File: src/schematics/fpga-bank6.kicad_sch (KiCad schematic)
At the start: 1 part

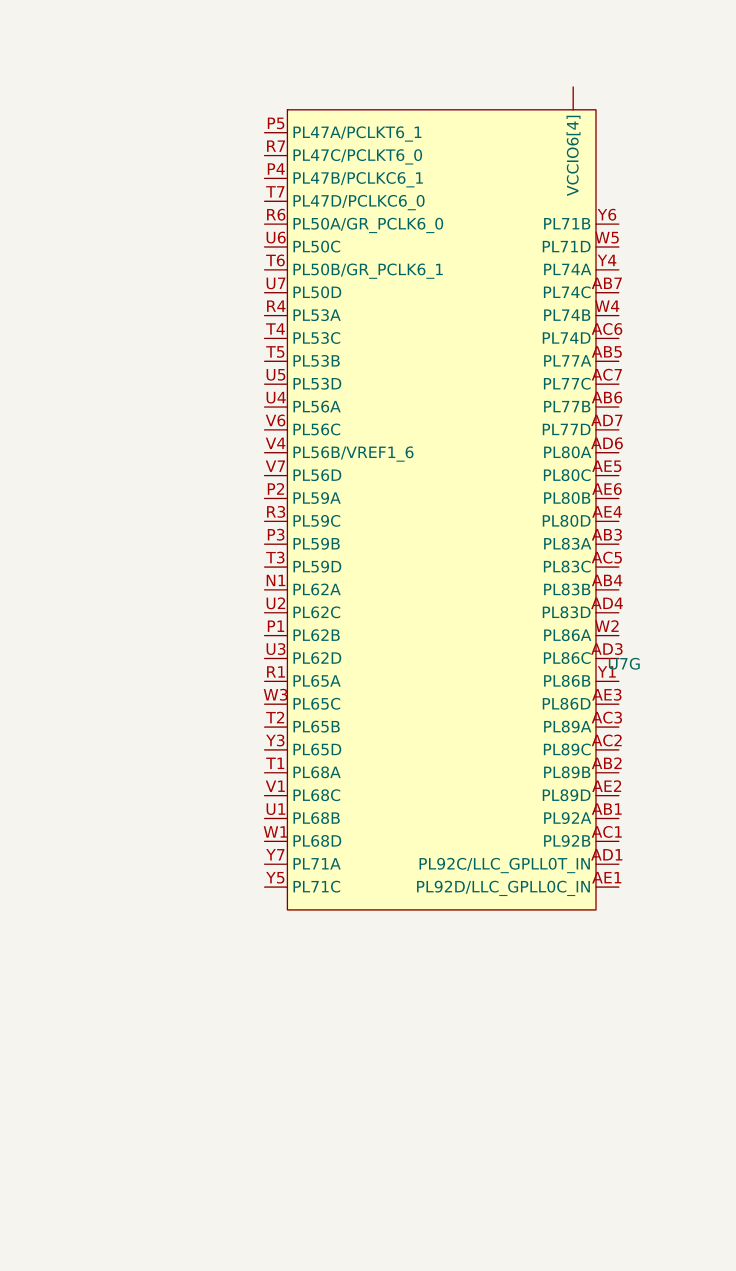
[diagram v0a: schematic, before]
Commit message: Draft connections between the FPGA and the memories
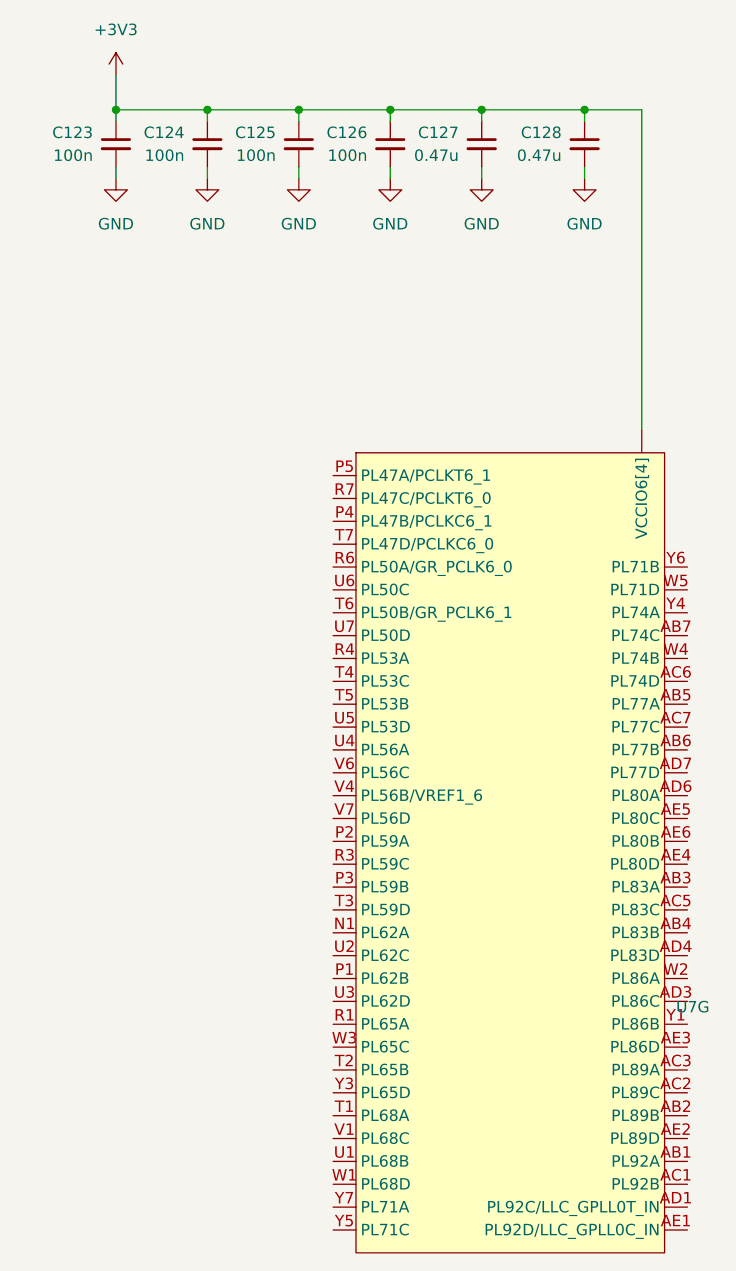
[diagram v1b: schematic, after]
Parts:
- added C123, C124, C125, C126: 100n, symbol Device:C_Small
- added C127, C128: 0.47u, symbol Device:C_Small
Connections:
- net VCCIO6 renamed +3V3
- net +3V3: now also C123.1, C124.1, C125.1, C126.1, C127.1, C128.1
- new net GND: C123.2, C124.2, C125.2, C126.2, C127.2, C128.2
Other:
- moved on the sheet: U7G

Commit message: Adds draft of IO connector schematic connections to FPGA
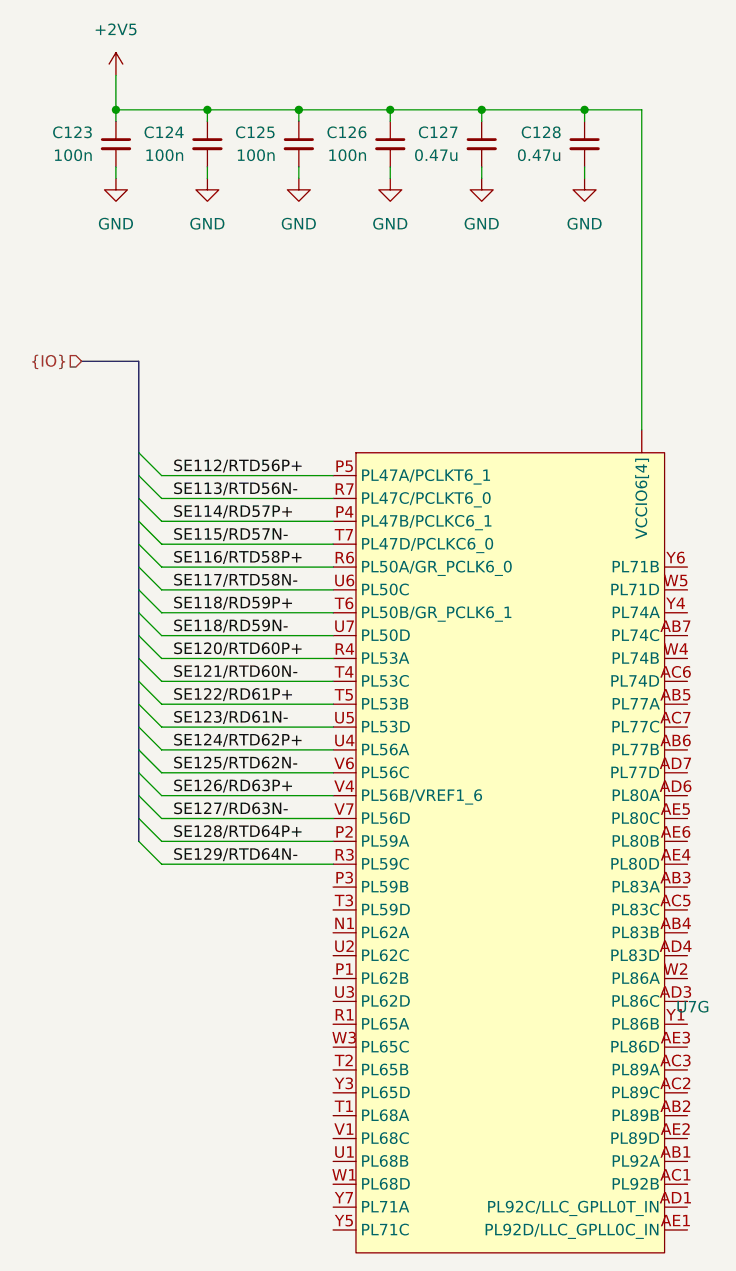
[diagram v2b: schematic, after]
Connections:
- net SE128/RTD64P+: now reaches U7.P2 (PL59A)
- net SE114/RD57P+: now reaches U7.P4 (PL47B/PCLKC6_1)
- net SE112/RTD56P+: now reaches U7.P5 (PL47A/PCLKT6_1)
- net SE129/RTD64N-: now reaches U7.R3 (PL59C)
- net SE120/RTD60P+: now reaches U7.R4 (PL53A)
- net SE116/RTD58P+: now reaches U7.R6 (PL50A/GR_PCLK6_0)
- net SE113/RTD56N-: now reaches U7.R7 (PL47C/PCLKT6_0)
- net SE121/RTD60N-: now reaches U7.T4 (PL53C)
- net SE122/RD61P+: now reaches U7.T5 (PL53B)
- net SE118/RD59P+: now reaches U7.T6 (PL50B/GR_PCLK6_1)
- net SE115/RD57N-: now reaches U7.T7 (PL47D/PCLKC6_0)
- net SE124/RTD62P+: now reaches U7.U4 (PL56A)
- net SE123/RD61N-: now reaches U7.U5 (PL53D)
- net SE117/RTD58N-: now reaches U7.U6 (PL50C)
- net SE118/RD59N-: now reaches U7.U7 (PL50D)
- net SE126/RD63P+: now reaches U7.V4 (PL56B/VREF1_6)
- net SE125/RTD62N-: now reaches U7.V6 (PL56C)
- net SE127/RD63N-: now reaches U7.V7 (PL56D)
- net +3V3 renamed +2V5

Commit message: Adds the clock oscillator
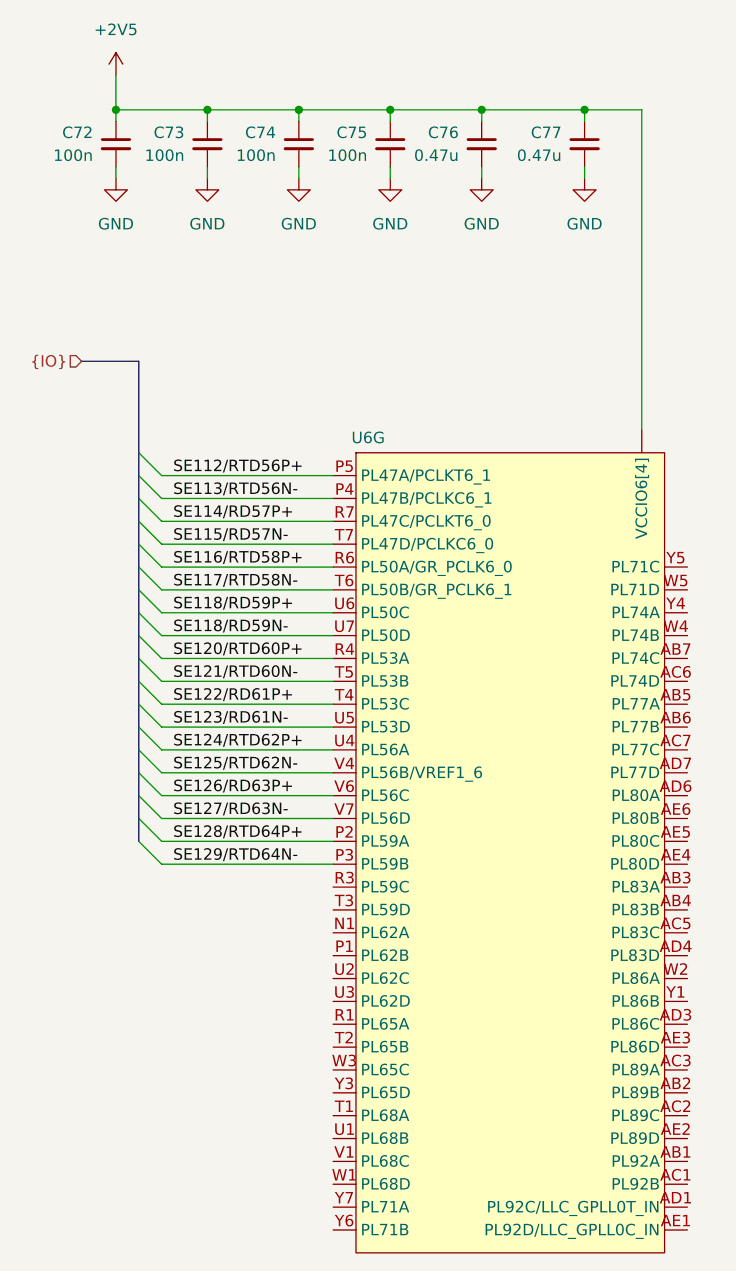
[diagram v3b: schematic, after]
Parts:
- removed U7: ~, symbol ECAP5-BSOM:LFE5U-85F-*BG756*
- added U6: ~, symbol ECAP5-BSOM:LFE5U-85F-*BG756*
- renumbered C123 to C72, C124 to C73, C125 to C74, C126 to C75, C127 to C76, C128 to C77
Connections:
- net +2V5: now also U6. (VCCIO6[4]), U6.AA10 (VCCIO6), U6.U10 (VCCIO6), U6.V10 (VCCIO6), U6.W10 (VCCIO6)
- net SE112/RTD56P+: now also U6.P5 (PL47A/PCLKT6_1)
- net SE113/RTD56N-: now also U6.P4 (PL47B/PCLKC6_1)
- net SE114/RD57P+: now also U6.R7 (PL47C/PCLKT6_0)
- net SE115/RD57N-: now also U6.T7 (PL47D/PCLKC6_0)
- net SE116/RTD58P+: now also U6.R6 (PL50A/GR_PCLK6_0)
- net SE117/RTD58N-: now also U6.T6 (PL50B/GR_PCLK6_1)
- net SE118/RD59N-: now also U6.U7 (PL50D)
- net SE118/RD59P+: now also U6.U6 (PL50C)
- net SE120/RTD60P+: now also U6.R4 (PL53A)
- net SE121/RTD60N-: now also U6.T5 (PL53B)
- net SE122/RD61P+: now also U6.T4 (PL53C)
- net SE123/RD61N-: now also U6.U5 (PL53D)
- net SE124/RTD62P+: now also U6.U4 (PL56A)
- net SE125/RTD62N-: now also U6.V4 (PL56B/VREF1_6)
- net SE126/RD63P+: now also U6.V6 (PL56C)
- net SE127/RD63N-: now also U6.V7 (PL56D)
- net SE128/RTD64P+: now also U6.P2 (PL59A)
- net SE129/RTD64N-: now also U6.P3 (PL59B)

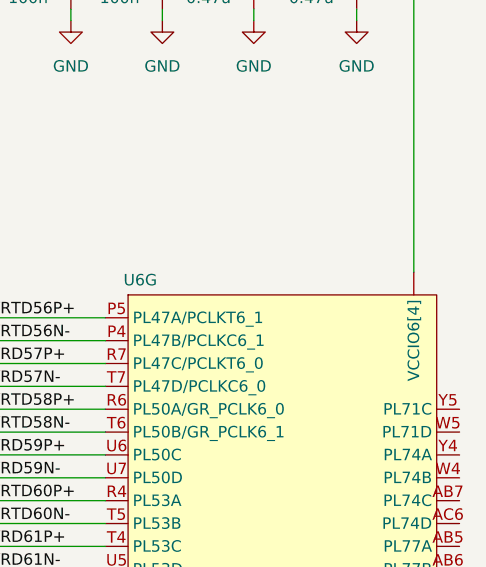
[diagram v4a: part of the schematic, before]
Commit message: Fix some ERC issues
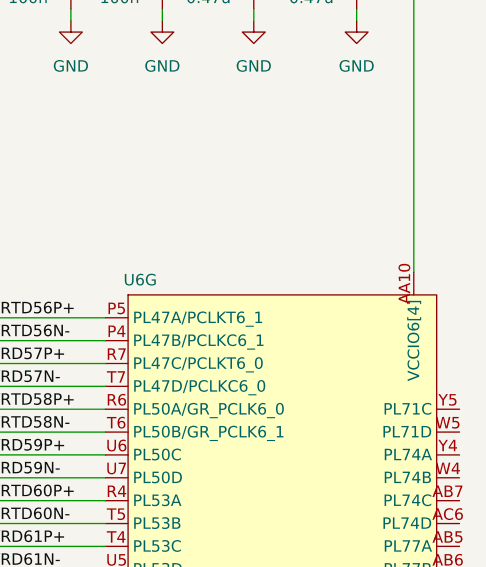
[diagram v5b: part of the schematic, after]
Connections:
- net +2V5: no longer U6. (VCCIO6[4])
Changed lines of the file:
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@@
 		(pin "Y31"
 		)
-		(pin ""
-		)
 		(pin "A10"
 		)
@@
 		(pin "Y32"
 		)
-		(pin ""
-		)
 		(pin "AB23"
 		)
@@
 		(pin "K16"
 		)
-		(pin ""
-		)
 		(pin "A18"
 		)
@@
 		(pin "K21"
 		)
-		(pin ""
-		)
 		(pin "B32"
 		)
@@
 		(pin "T23"
 		)
-		(pin ""
-		)
 		(pin "AA23"
 		)
@@
 		(pin "AM31"
 		)
-		(pin ""
-		)
 		(pin "AA10"
 		)
@@
 		(pin "Y7"
 		)
-		(pin ""
-		)
 		(pin "B1"
 		)
@@
 		(pin "T10"
 		)
-		(pin ""
-		)
 		(pin "AB10"
 		)
@@
 		(pin "M14"
 		)
-		(pin ""
-		)
 		(pin "AH12"
 		)
@@
 		(pin "V19"
 		)
-		(pin ""
-		)
 		(pin "AC11"
 		)
@@
 		(pin "AA11"
 		)
-		(pin ""
-		)
 		(instances

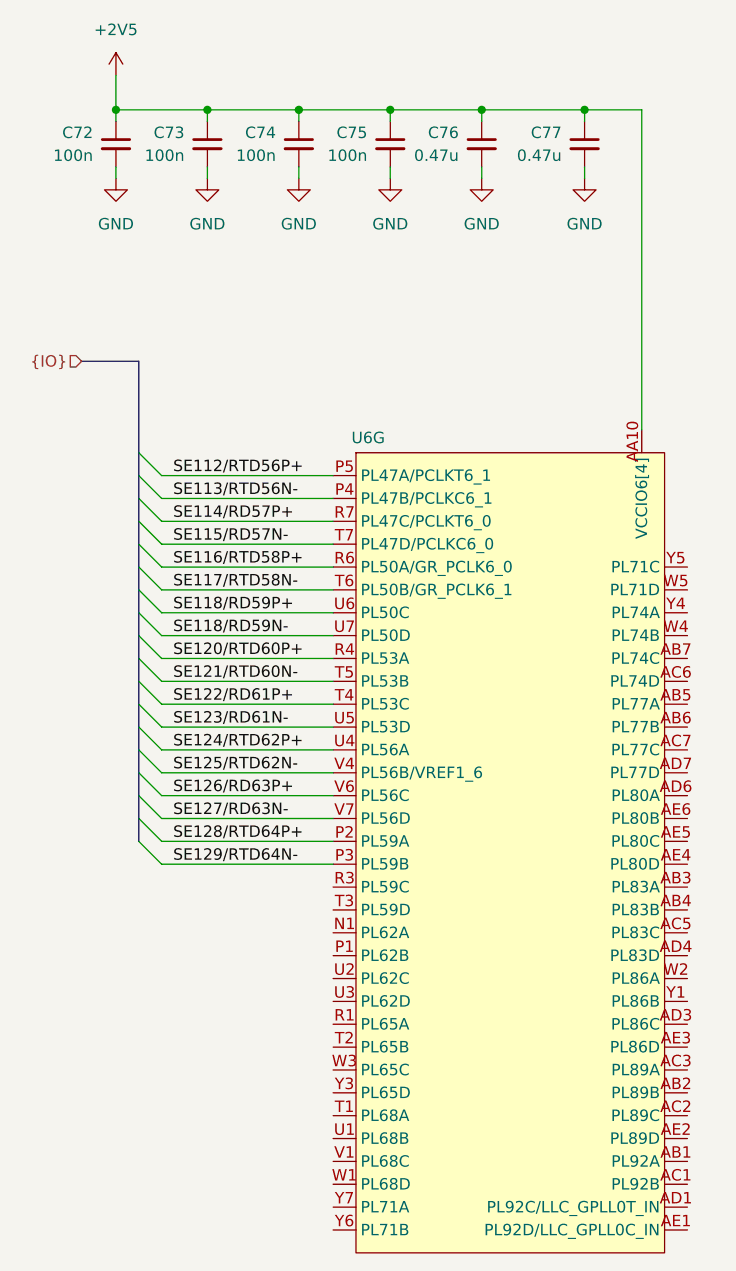
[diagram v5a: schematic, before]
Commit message: Fixes bus aliases
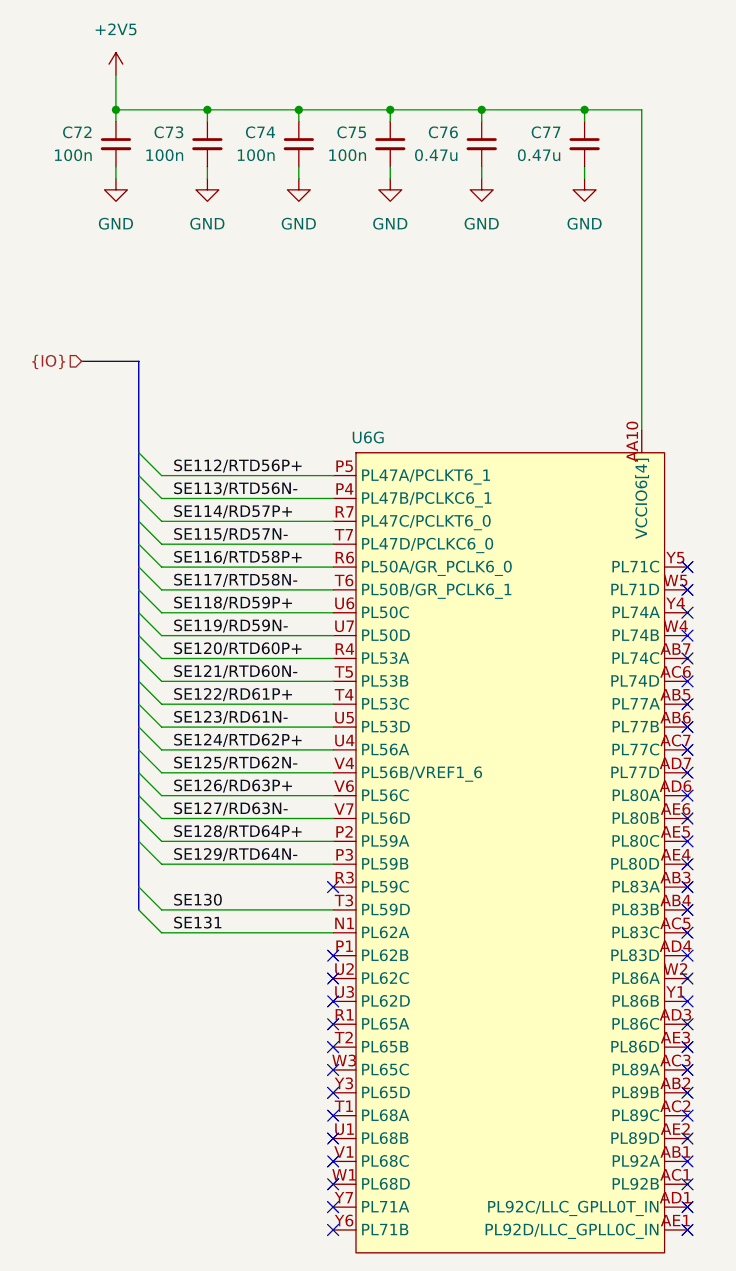
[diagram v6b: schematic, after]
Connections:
- net SE131: now reaches U6.N1 (PL62A)
- net SE130: now reaches U6.T3 (PL59D)
- net SE118/RD59N- renamed SE119/RD59N-
- no-connect marks 0 -> 44
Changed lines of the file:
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@@
 		(color 0 0 0 0)
+	)
+	(no_connect
+		(at 181.61 120.65)
+	)
+	(no_connect
+		(at 142.24 143.51)
+	)
+	(no_connect
+		(at 181.61 156.21)
+	)
+	(no_connect
+		(at 181.61 102.87)
+	)
+	(no_connect
+		(at 142.24 140.97)
+	)
+	(no_connect
+		(at 142.24 156.21)
+	)
+	(no_connect
+		(at 181.61 97.79)
+	)
+	(no_connect
+		(at 181.61 107.95)
+	)
+	(no_connect
+		(at 142.24 151.13)
+	)
+	(no_connect
+		(at 181.61 95.25)
+	)
+	(no_connect
+		(at 181.61 118.11)
+	)
+	(no_connect
+		(at 181.61 125.73)
+	)
+	(no_connect
+		(at 181.61 115.57)
+	)
+	(no_connect
+		(at 142.24 133.35)
+	)
+	(no_connect
+		(at 181.61 87.63)
+	)
+	(no_connect
+		(at 181.61 138.43)
+	)
+	(no_connect
+		(at 181.61 100.33)
+	)
+	(no_connect
+		(at 181.61 151.13)
+	)
+	(no_connect
+		(at 181.61 130.81)
+	)
+	(no_connect
+		(at 181.61 105.41)
+	)
+	(no_connect
+		(at 142.24 138.43)
+	)
+	(no_connect
+		(at 181.61 140.97)
+	)
+	(no_connect
+		(at 181.61 135.89)
+	)
+	(no_connect
+		(at 181.61 82.55)
+	)
+	(no_connect
+		(at 181.61 85.09)
+	)
+	(no_connect
+		(at 142.24 130.81)
+	)
+	(no_connect
+		(at 181.61 128.27)
+	)
+	(no_connect
+		(at 181.61 113.03)
+	)
+	(no_connect
+		(at 181.61 90.17)
+	)
+	(no_connect
+		(at 142.24 148.59)
+	)
+	(no_connect
+		(at 142.24 153.67)
+	)
+	(no_connect
+		(at 181.61 92.71)
+	)
+	(no_connect
+		(at 181.61 153.67)
+	)
+	(no_connect
+		(at 181.61 146.05)
+	)
+	(no_connect
+		(at 181.61 148.59)
+	)
+	(no_connect
+		(at 181.61 143.51)
+	)
+	(no_connect
+		(at 142.24 128.27)
+	)
+	(no_connect
+		(at 142.24 118.11)
+	)
+	(no_connect
+		(at 181.61 110.49)
+	)
+	(no_connect
+		(at 181.61 133.35)
+	)
+	(no_connect
+		(at 142.24 135.89)
+	)
+	(no_connect
+		(at 142.24 125.73)
+	)
+	(no_connect
+		(at 142.24 146.05)
+	)
+	(no_connect
+		(at 181.61 123.19)
 	)
 	(bus_entry
@@
 	)
 	(bus_entry
+		(at 120.65 118.11)
+		(size 2.54 2.54)
+		(stroke
+			(width 0)
+			(type default)
+		)
+	)
+	(bus_entry
 		(at 120.65 90.17)
 		(size 2.54 2.54)
@@
 	)
 	(bus_entry
+		(at 120.65 120.65)
+		(size 2.54 2.54)
+		(stroke
+			(width 0)
+			(type default)
+		)
+	)
+	(bus_entry
 		(at 120.65 92.71)
 		(size 2.54 2.54)
@@
 	(wire
 		(pts
+			(xy 123.19 120.65) (xy 142.24 120.65)
+		)
+		(stroke
+			(width 0)
+			(type default)
+		)
+	)
+	(wire
+		(pts
 			(xy 123.19 90.17) (xy 142.24 90.17)
 		)
@@
 		)
 	)
+	(bus
+		(pts
+			(xy 120.65 113.03) (xy 120.65 118.11)
+		)
+		(stroke
+			(width 0)
+			(type default)
+		)
+	)
 	(wire
 		(pts
@@
 		(pts
 			(xy 128.27 31.75) (xy 128.27 33.02)
+		)
+		(stroke
+			(width 0)
+			(type default)
+		)
+	)
+	(wire
+		(pts
+			(xy 123.19 123.19) (xy 142.24 123.19)
+		)
+		(stroke
+			(width 0)
+			(type default)
+		)
+	)
+	(bus
+		(pts
+			(xy 120.65 118.11) (xy 120.65 120.65)
 		)
 		(stroke
@@
 		)
 	)
-	(label "SE118{slash}RD59N-"
+	(label "SE119{slash}RD59N-"
 		(at 124.46 90.17 0)
 		(fields_autoplaced yes)
@@
 		)
 	)
-	(label "SE114{slash}RD57P+"
-		(at 124.46 77.47 0)
+	(label "SE130"
+		(at 124.46 120.65 0)
 		(fields_autoplaced yes)
 		(effects
@@
 		)
 	)
-	(label "SE128{slash}RTD64P+"
-		(at 124.46 113.03 0)
+	(label "SE114{slash}RD57P+"
+		(at 124.46 77.47 0)
 		(fields_autoplaced yes)
 		(effects
@@
 		)
 	)
-	(label "SE129{slash}RTD64N-"
-		(at 124.46 115.57 0)
+	(label "SE128{slash}RTD64P+"
+		(at 124.46 113.03 0)
 		(fields_autoplaced yes)
 		(effects
@@
 		)
 	)
-	(label "SE127{slash}RD63N-"
-		(at 124.46 110.49 0)
+	(label "SE129{slash}RTD64N-"
+		(at 124.46 115.57 0)
 		(fields_autoplaced yes)
 		(effects
@@
 		)
 	)
-	(label "SE112{slash}RTD56P+"
-		(at 124.46 72.39 0)
+	(label "SE127{slash}RD63N-"
+		(at 124.46 110.49 0)
 		(fields_autoplaced yes)
 		(effects
@@
 		)
 	)
-	(label "SE115{slash}RD57N-"
-		(at 124.46 80.01 0)
+	(label "SE112{slash}RTD56P+"
+		(at 124.46 72.39 0)
 		(fields_autoplaced yes)
 		(effects
@@
 		)
 	)
-	(label "SE125{slash}RTD62N-"
-		(at 124.46 105.41 0)
+	(label "SE115{slash}RD57N-"
+		(at 124.46 80.01 0)
 		(fields_autoplaced yes)
 		(effects
@@
 		)
 	)
-	(label "SE113{slash}RTD56N-"
-		(at 124.46 74.93 0)
+	(label "SE125{slash}RTD62N-"
+		(at 124.46 105.41 0)
 		(fields_autoplaced yes)
 		(effects
@@
 		)
 	)
-	(label "SE116{slash}RTD58P+"
-		(at 124.46 82.55 0)
+	(label "SE113{slash}RTD56N-"
+		(at 124.46 74.93 0)
 		(fields_autoplaced yes)
 		(effects
@@
 		)
 	)
-	(label "SE123{slash}RD61N-"
-		(at 124.46 100.33 0)
+	(label "SE116{slash}RTD58P+"
+		(at 124.46 82.55 0)
 		(fields_autoplaced yes)
 		(effects
@@
 		)
 	)
+	(label "SE123{slash}RD61N-"
+		(at 124.46 100.33 0)
+		(fields_autoplaced yes)
+		(effects
+			(font
+				(size 1.27 1.27)
+			)
+			(justify left bottom)
+		)
+	)
 	(label "SE120{slash}RTD60P+"
 		(at 124.46 92.71 0)
+		(fields_autoplaced yes)
+		(effects
+			(font
+				(size 1.27 1.27)
+			)
+			(justify left bottom)
+		)
+	)
+	(label "SE131"
+		(at 124.46 123.19 0)
 		(fields_autoplaced yes)
 		(effects
@@
 		(pin "AB32"
 		)
-		(pin "AB32"
+		(pin "AB31"
 		)
 		(pin "AC26"
